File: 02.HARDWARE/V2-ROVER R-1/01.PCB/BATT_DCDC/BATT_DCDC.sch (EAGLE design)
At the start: 63 parts, among them J1 DF40C-20DP-0.4V_51_, K1 FLEX11, Q1 NVTFS9D6P04M8LTAG, Q2 2N7002PW, Q3 2N7002PW, U1 MCP6071T-E/OT, U2 LM5114BMF_NOPB, U3 TPS55330RTET, U7 MCP6071T-E/OT

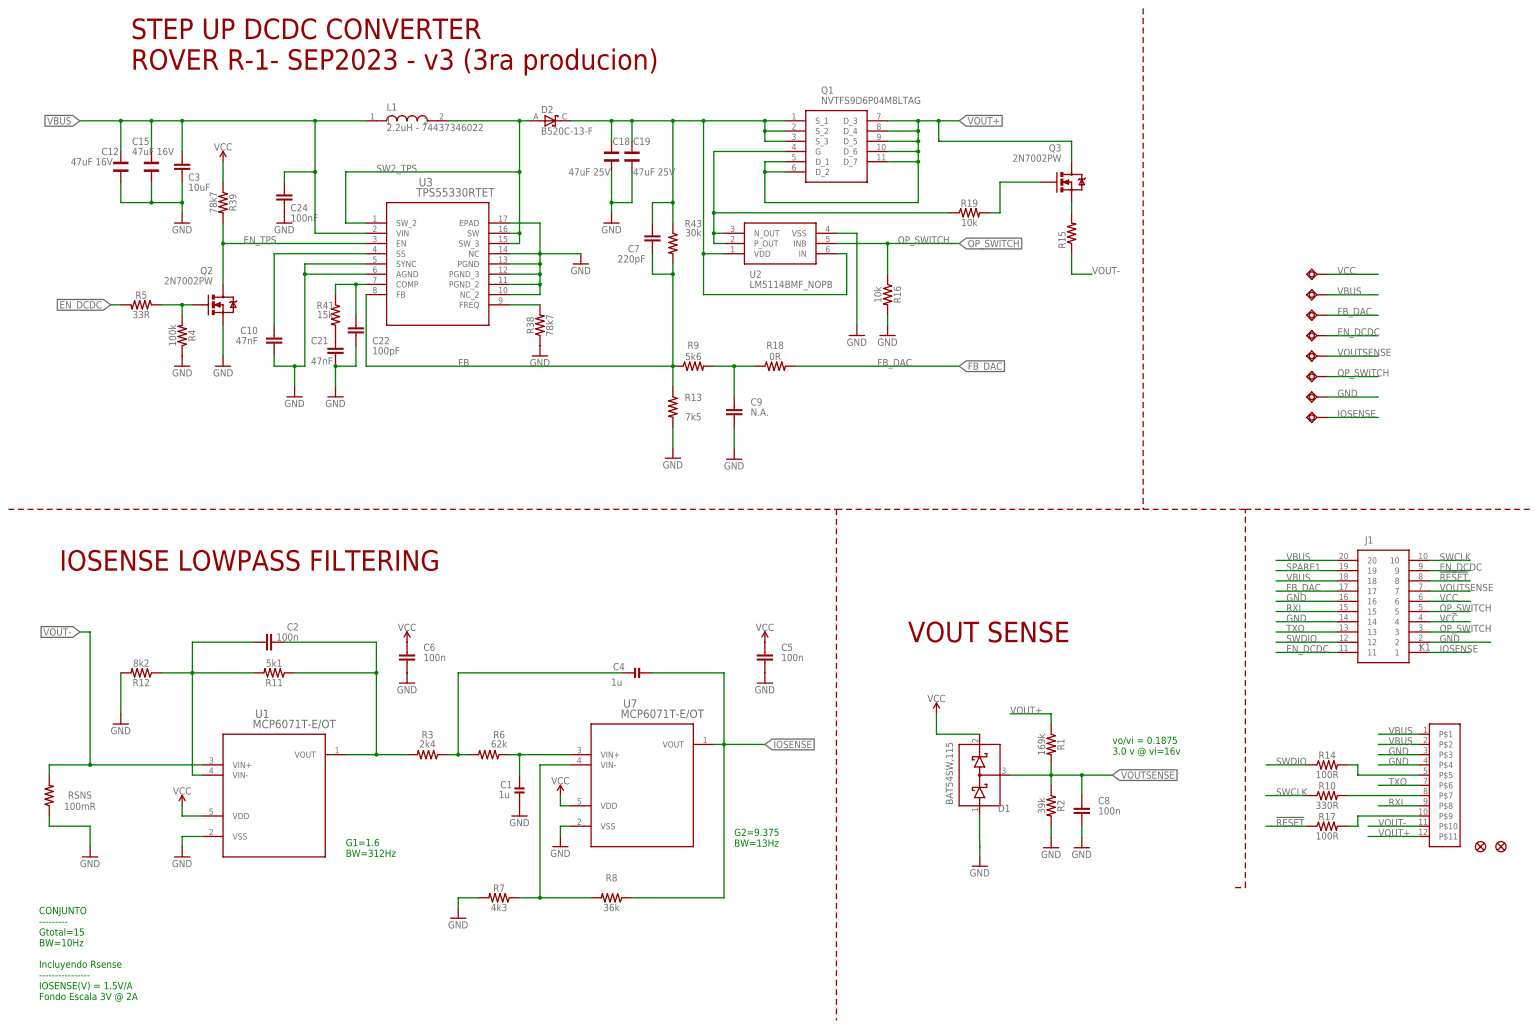
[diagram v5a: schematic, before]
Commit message: Correccion errores e inclusion Fiducial Marks en DCDC
Se divide en 2 la RBalastro.
Recolocación a parte superior.
Inclusión 2 fiduciales en la parte del botom
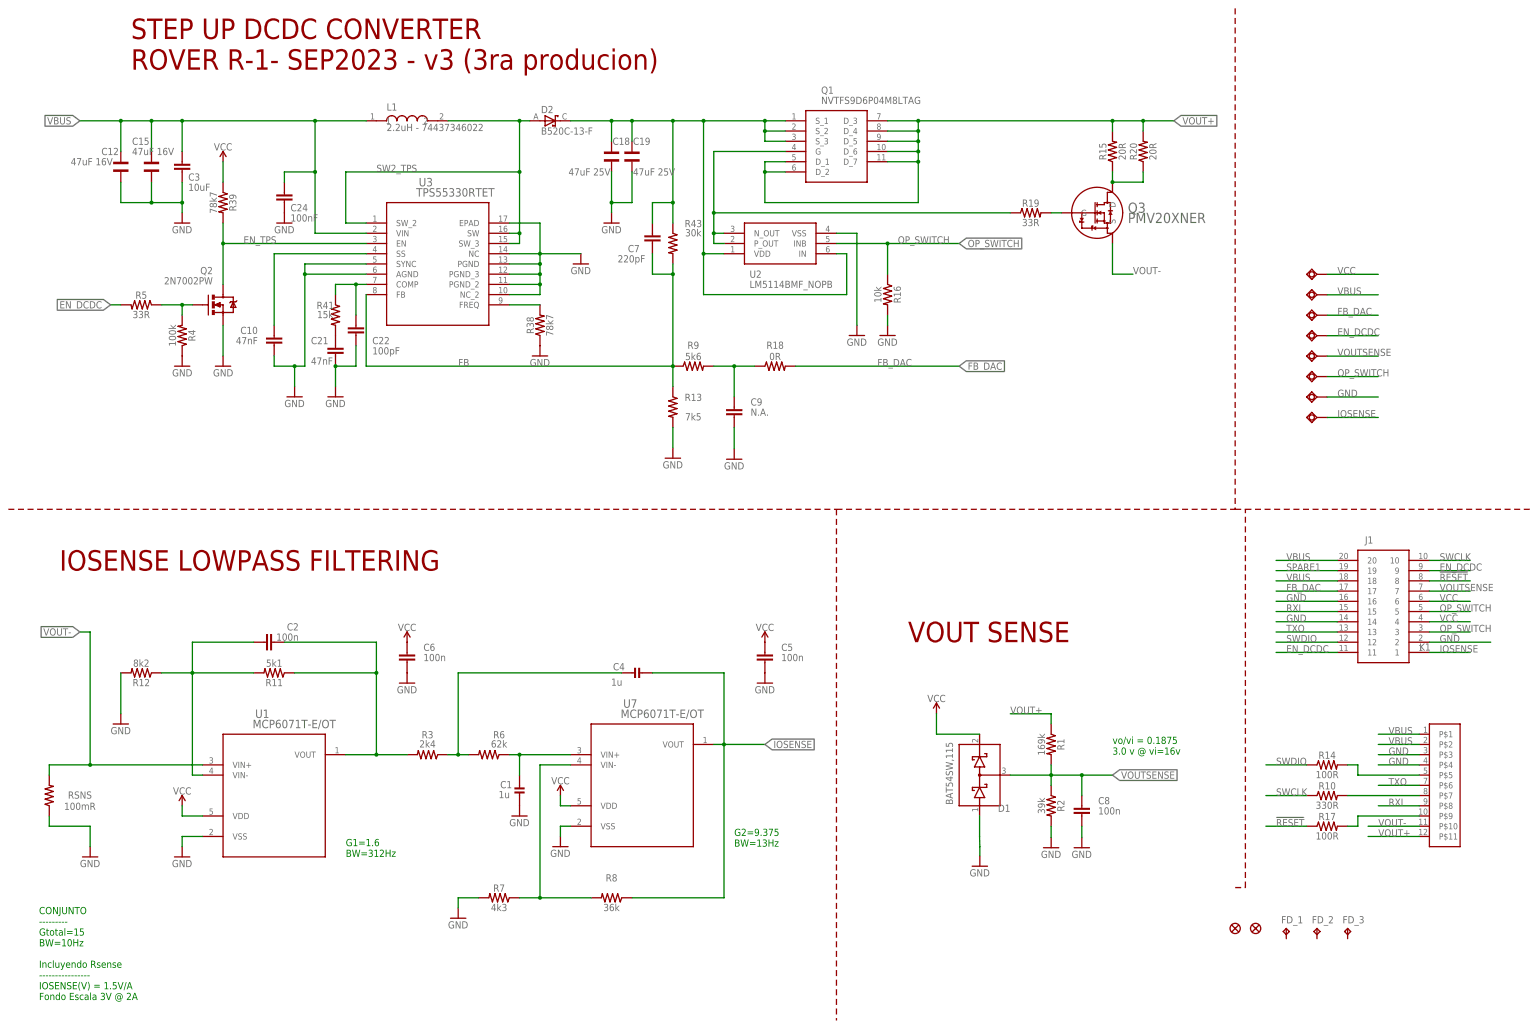
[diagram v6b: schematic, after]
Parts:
- added FD_1, FD_2, FD_3: FD_1, testpad:TPTP06SQ
- added R20: 20R, SparkFun-Resistors:RESISTOR1206
- Q3: value 2N7002PW -> PMV20XNER; device SparkFun-DiscreteSemi:MOSFET-NCHANNEL2N7002PW -> PMV20XNER:PMV20XNERSOT23-TO-236AB_NEX-L
- R15: value (none) -> 20R; device adafruit:R-US_R2512 -> SparkFun-Resistors:RESISTOR1206
- R19: value 10k -> 33R
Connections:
- net N$8: now also Q3.D, R15.1, R20.1; no longer Q3.S, R15.2
- net VOUT+: now also R15.2, R20.2; no longer Q3.D
- net VOUT-: now also Q3.S; no longer R15.1
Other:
- moved on the sheet: R15, R19
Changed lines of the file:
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@@
 <part name="U2" library="LM5114BMF_NOPB" deviceset="LM5114BMF_NOPB" device=""/>
 <part name="GND2" library="SparkFun" deviceset="GND" device=""/>
-<part name="R15" library="adafruit" library_urn="urn:adsk.eagle:library:420" deviceset="R-US_" device="R2512" package3d_urn="urn:adsk.eagle:package:6240577/1"/>
-<part name="Q3" library="SparkFun-DiscreteSemi" deviceset="MOSFET-NCHANNEL" device="2N7002PW" value="2N7002PW"/>
-<part name="R19" library="SparkFun-Resistors" library_urn="urn:adsk.eagle:library:532" deviceset="RESISTOR" device="0402" package3d_urn="urn:adsk.eagle:package:39657/1" value="10k"/>
+<part name="R15" library="SparkFun-Resistors" library_urn="urn:adsk.eagle:library:532" deviceset="RESISTOR" device="1206" package3d_urn="urn:adsk.eagle:package:39654/1" value="20R"/>
+<part name="Q3" library="PMV20XNER" deviceset="PMV20XNER" device="SOT23-TO-236AB_NEX-L" value="PMV20XNER"/>
+<part name="R19" library="SparkFun-Resistors" library_urn="urn:adsk.eagle:library:532" deviceset="RESISTOR" device="0402" package3d_urn="urn:adsk.eagle:package:39657/1" value="33R"/>
+<part name="R20" library="SparkFun-Resistors" library_urn="urn:adsk.eagle:library:532" deviceset="RESISTOR" device="1206" package3d_urn="urn:adsk.eagle:package:39654/1" value="20R"/>
+<part name="FD_1" library="testpad" library_urn="urn:adsk.eagle:library:385" deviceset="TP" device="TP06SQ" package3d_urn="urn:adsk.eagle:package:27952/1" value="FD_1"/>
+<part name="FD_2" library="testpad" library_urn="urn:adsk.eagle:library:385" deviceset="TP" device="TP06SQ" package3d_urn="urn:adsk.eagle:package:27952/1" value="FD_1"/>
+<part name="FD_3" library="testpad" library_urn="urn:adsk.eagle:library:385" deviceset="TP" device="TP06SQ" package3d_urn="urn:adsk.eagle:package:27952/1" value="FD_1"/>
 </parts>
 <sheets>
@@
 BW=13Hz</text>
 <wire x1="5.08" y1="132.08" x2="210.82" y2="132.08" width="0.1524" layer="94" style="shortdash"/>
-<wire x1="210.82" y1="132.08" x2="287.02" y2="132.08" width="0.1524" layer="94" style="shortdash"/>
-<wire x1="287.02" y1="132.08" x2="312.42" y2="132.08" width="0.1524" layer="94" style="shortdash"/>
+<wire x1="210.82" y1="132.08" x2="309.88" y2="132.08" width="0.1524" layer="94" style="shortdash"/>
+<wire x1="309.88" y1="132.08" x2="312.42" y2="132.08" width="0.1524" layer="94" style="shortdash"/>
 <wire x1="312.42" y1="132.08" x2="383.54" y2="132.08" width="0.1524" layer="94" style="shortdash"/>
-<wire x1="287.02" y1="256.54" x2="287.02" y2="132.08" width="0.1524" layer="94" style="shortdash"/>
+<wire x1="309.88" y1="256.54" x2="309.88" y2="132.08" width="0.1524" layer="94" style="shortdash"/>
 <wire x1="210.82" y1="132.08" x2="210.82" y2="5.08" width="0.1524" layer="94" style="shortdash"/>
 <wire x1="309.88" y1="38.1" x2="312.42" y2="38.1" width="0.1524" layer="94" style="shortdash"/>
@@
 <attribute name="VALUE" x="49.784" y="212.979" size="1.778" layer="96" font="vector" rot="MR180"/>
 </instance>
-<instance part="U$1" gate="G$1" x="370.84" y="48.26" smashed="yes"/>
-<instance part="U$2" gate="G$1" x="375.92" y="48.26" smashed="yes"/>
+<instance part="U$1" gate="G$1" x="309.88" y="27.94" smashed="yes"/>
+<instance part="U$2" gate="G$1" x="314.96" y="27.94" smashed="yes"/>
 <instance part="R1" gate="G$1" x="264.16" y="73.66" smashed="yes" rot="R270">
 <attribute name="NAME" x="265.684" y="73.66" size="1.778" layer="95" font="vector" rot="R270" align="bottom-center"/>
@@
 <attribute name="VALUE" x="213.36" y="172.72" size="1.778" layer="96"/>
 </instance>
-<instance part="R15" gate="G$1" x="269.24" y="200.66" smashed="yes" rot="R90">
-<attribute name="NAME" x="267.7414" y="196.85" size="1.778" layer="95" rot="R90"/>
-<attribute name="VALUE" x="272.542" y="196.85" size="1.778" layer="96" rot="R90"/>
-</instance>
-<instance part="Q3" gate="G$1" x="269.24" y="213.36" smashed="yes">
-<attribute name="NAME" x="266.7" y="220.98" size="1.778" layer="95" rot="MR0"/>
-<attribute name="VALUE" x="266.7" y="218.44" size="1.778" layer="96" rot="MR0"/>
-</instance>
-<instance part="R19" gate="G$1" x="243.84" y="205.74" smashed="yes">
-<attribute name="NAME" x="243.84" y="207.264" size="1.778" layer="95" font="vector" align="bottom-center"/>
-<attribute name="VALUE" x="243.84" y="204.216" size="1.778" layer="96" font="vector" align="top-center"/>
+<instance part="R15" gate="G$1" x="279.4" y="220.98" smashed="yes" rot="R90">
+<attribute name="NAME" x="277.876" y="220.98" size="1.778" layer="95" font="vector" rot="R90" align="bottom-center"/>
+<attribute name="VALUE" x="280.924" y="220.98" size="1.778" layer="96" font="vector" rot="R90" align="top-center"/>
+</instance>
+<instance part="Q3" gate="A" x="266.7" y="205.74" smashed="yes">
+<attribute name="NAME" x="283.21" y="205.74" size="2.54" layer="95" ratio="10" rot="SR0"/>
+<attribute name="VALUE" x="283.21" y="203.2" size="2.54" layer="96" ratio="10" rot="SR0"/>
+</instance>
+<instance part="R19" gate="G$1" x="259.08" y="205.74" smashed="yes">
+<attribute name="NAME" x="259.08" y="207.264" size="1.778" layer="95" font="vector" align="bottom-center"/>
+<attribute name="VALUE" x="259.08" y="204.216" size="1.778" layer="96" font="vector" align="top-center"/>
+</instance>
+<instance part="R20" gate="G$1" x="287.02" y="220.98" smashed="yes" rot="R90">
+<attribute name="NAME" x="285.496" y="220.98" size="1.778" layer="95" font="vector" rot="R90" align="bottom-center"/>
+<attribute name="VALUE" x="288.544" y="220.98" size="1.778" layer="96" font="vector" rot="R90" align="top-center"/>
+</instance>
+<instance part="FD_1" gate="G$1" x="322.58" y="27.94" smashed="yes">
+<attribute name="NAME" x="321.31" y="29.21" size="1.778" layer="95"/>
+<attribute name="TP_SIGNAL_NAME" x="323.85" y="26.67" size="1.778" layer="97"/>
+</instance>
+<instance part="FD_2" gate="G$1" x="330.2" y="27.94" smashed="yes">
+<attribute name="NAME" x="328.93" y="29.21" size="1.778" layer="95"/>
+<attribute name="TP_SIGNAL_NAME" x="331.47" y="26.67" size="1.778" layer="97"/>
+</instance>
+<instance part="FD_3" gate="G$1" x="337.82" y="27.94" smashed="yes">
+<attribute name="NAME" x="336.55" y="29.21" size="1.778" layer="95"/>
+<attribute name="TP_SIGNAL_NAME" x="339.09" y="26.67" size="1.778" layer="97"/>
 </instance>
 </instances>
@@
 <wire x1="231.14" y1="208.28" x2="231.14" y2="218.44" width="0.1524" layer="91"/>
 <junction x="231.14" y="218.44"/>
-<label x="241.3" y="228.6" size="1.778" layer="95" xref="yes"/>
-<wire x1="231.14" y1="228.6" x2="236.22" y2="228.6" width="0.1524" layer="91"/>
+<label x="294.64" y="228.6" size="1.778" layer="95" xref="yes"/>
+<wire x1="231.14" y1="228.6" x2="279.4" y2="228.6" width="0.1524" layer="91"/>
 <junction x="231.14" y="228.6"/>
-<wire x1="236.22" y1="228.6" x2="241.3" y2="228.6" width="0.1524" layer="91"/>
-<wire x1="236.22" y1="223.52" x2="236.22" y2="228.6" width="0.1524" layer="91"/>
-<junction x="236.22" y="228.6"/>
-<pinref part="Q3" gate="G$1" pin="D"/>
-<wire x1="269.24" y1="218.44" x2="269.24" y2="223.52" width="0.1524" layer="91"/>
-<wire x1="269.24" y1="223.52" x2="236.22" y2="223.52" width="0.1524" layer="91"/>
+<wire x1="279.4" y1="228.6" x2="287.02" y2="228.6" width="0.1524" layer="91"/>
+<wire x1="287.02" y1="228.6" x2="294.64" y2="228.6" width="0.1524" layer="91"/>
+<wire x1="279.4" y1="226.06" x2="279.4" y2="228.6" width="0.1524" layer="91"/>
+<junction x="279.4" y="228.6"/>
+<pinref part="R15" gate="G$1" pin="2"/>
+<pinref part="R20" gate="G$1" pin="2"/>
+<wire x1="287.02" y1="226.06" x2="287.02" y2="228.6" width="0.1524" layer="91"/>
+<junction x="287.02" y="228.6"/>
 </segment>
 <segment>
@@
 </segment>
 <segment>
-<pinref part="R15" gate="G$1" pin="1"/>
-<wire x1="269.24" y1="195.58" x2="269.24" y2="190.5" width="0.1524" layer="91"/>
-<wire x1="269.24" y1="190.5" x2="274.32" y2="190.5" width="0.1524" layer="91"/>
-<label x="274.32" y="190.5" size="1.778" layer="95"/>
+<wire x1="279.4" y1="190.5" x2="284.48" y2="190.5" width="0.1524" layer="91"/>
+<label x="284.48" y="190.5" size="1.778" layer="95"/>
+<pinref part="Q3" gate="A" pin="S"/>
+<wire x1="279.4" y1="198.12" x2="279.4" y2="190.5" width="0.1524" layer="91"/>
 </segment>
 </net>
@@
 <wire x1="180.34" y1="198.12" x2="182.88" y2="198.12" width="0.1524" layer="91"/>
 <pinref part="R19" gate="G$1" pin="1"/>
-<wire x1="180.34" y1="205.74" x2="238.76" y2="205.74" width="0.1524" layer="91"/>
+<wire x1="180.34" y1="205.74" x2="254" y2="205.74" width="0.1524" layer="91"/>
 <junction x="180.34" y="205.74"/>
 </segment>
 </net>
+<net name="N$13" class="0">
+<segment>
+<pinref part="Q3" gate="A" pin="G"/>
+<wire x1="264.16" y1="205.74" x2="266.7" y2="205.74" width="0.1524" layer="91"/>
+<pinref part="R19" gate="G$1" pin="2"/>
+</segment>
+</net>
 <net name="N$8" class="0">
 <segment>
-<pinref part="R15" gate="G$1" pin="2"/>
-<wire x1="269.24" y1="205.74" x2="269.24" y2="208.28" width="0.1524" layer="91"/>
-<pinref part="Q3" gate="G$1" pin="S"/>
-</segment>
-</net>
-<net name="N$13" class="0">
-<segment>
-<pinref part="Q3" gate="G$1" pin="G"/>
-<wire x1="251.46" y1="213.36" x2="261.62" y2="213.36" width="0.1524" layer="91"/>
-<wire x1="251.46" y1="205.74" x2="251.46" y2="213.36" width="0.1524" layer="91"/>
-<pinref part="R19" gate="G$1" pin="2"/>
-<wire x1="248.92" y1="205.74" x2="251.46" y2="205.74" width="0.1524" layer="91"/>
-</segment>
-</net>
+<pinref part="R15" gate="G$1" pin="1"/>
+<pinref part="Q3" gate="A" pin="D"/>
+<wire x1="279.4" y1="215.9" x2="279.4" y2="213.36" width="0.1524" layer="91"/>
+<pinref part="R20" gate="G$1" pin="1"/>
+<wire x1="287.02" y1="215.9" x2="287.02" y2="213.36" width="0.1524" layer="91"/>
+<wire x1="287.02" y1="213.36" x2="279.4" y2="213.36" width="0.1524" layer="91"/>
+<junction x="279.4" y="213.36"/>
+</segment>
+</net>

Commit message: Adiccion de Fiducidiales y actualizacion de Version
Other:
- note added: "STEP UP DCDC CONVERTER ROVER R-1- Nov'23 v5"
- note removed: "STEP UP DCDC CONVERTER ROVER R-1- SEP2023 - v3 (3ra producion)"
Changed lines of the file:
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@@
 <text x="17.78" y="116.84" size="5.08" layer="94">IOSENSE LOWPASS FILTERING</text>
 <text x="35.56" y="241.3" size="5.08" layer="94">STEP UP DCDC CONVERTER
-ROVER R-1- SEP2023 - v3 (3ra producion)</text>
+ROVER R-1- Nov'23 v5</text>
 <text x="88.9" y="45.72" size="1.778" layer="91">G1=1.6
 BW=312Hz</text>
